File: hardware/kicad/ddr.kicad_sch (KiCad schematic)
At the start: 2 parts, among them U202 xc7z007sclg225, U301 MT41K256M16TW-107_P

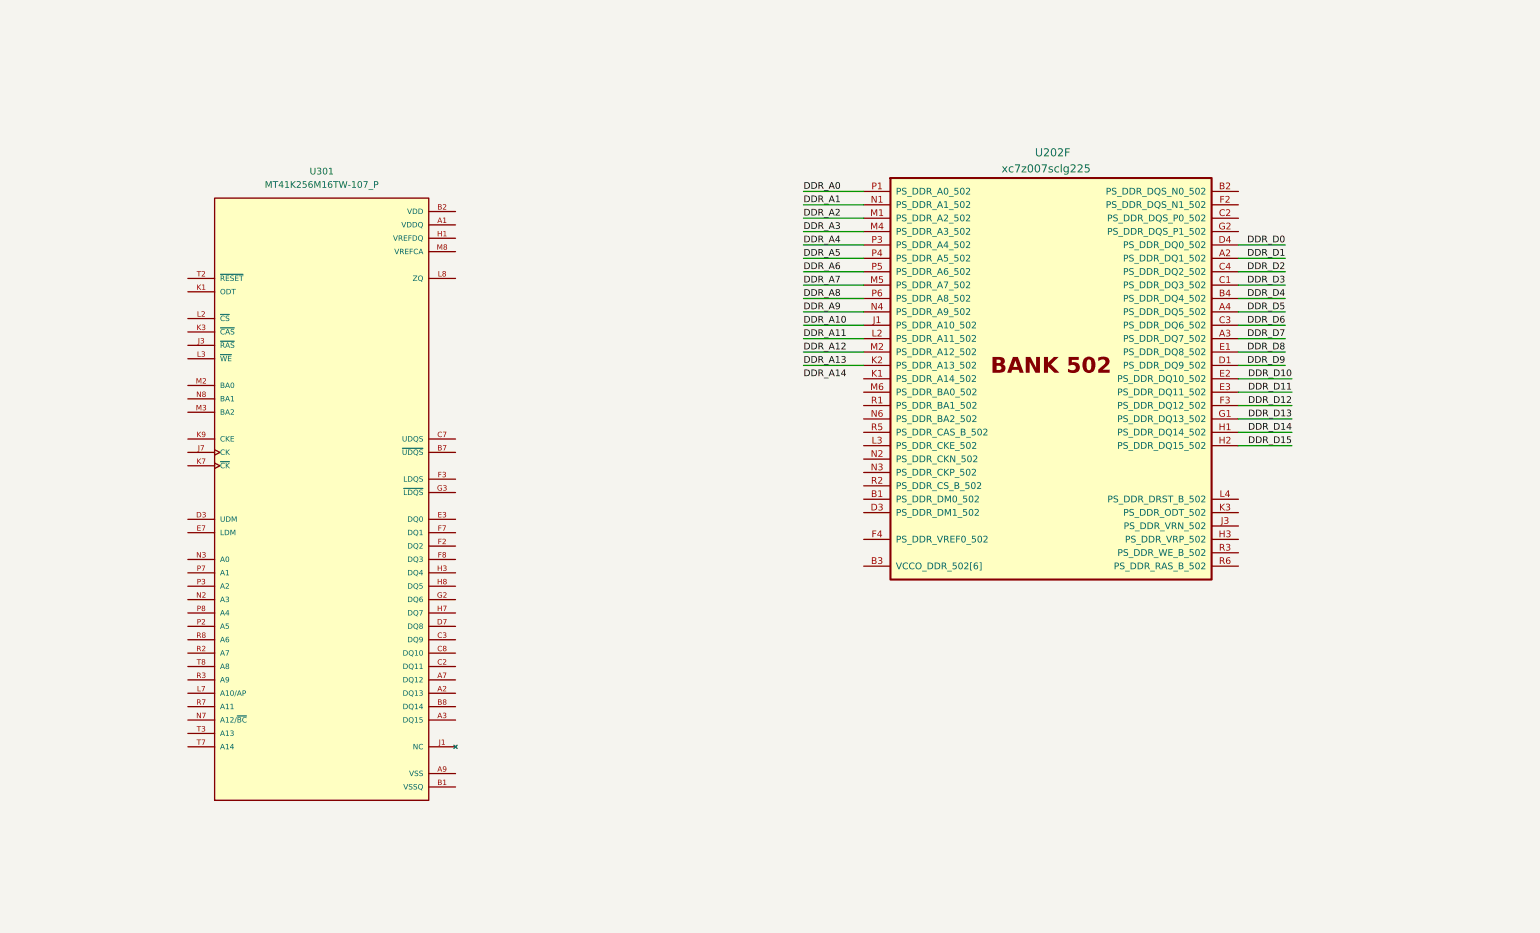
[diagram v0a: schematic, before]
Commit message: layout: finish dq0 & dq1 routing
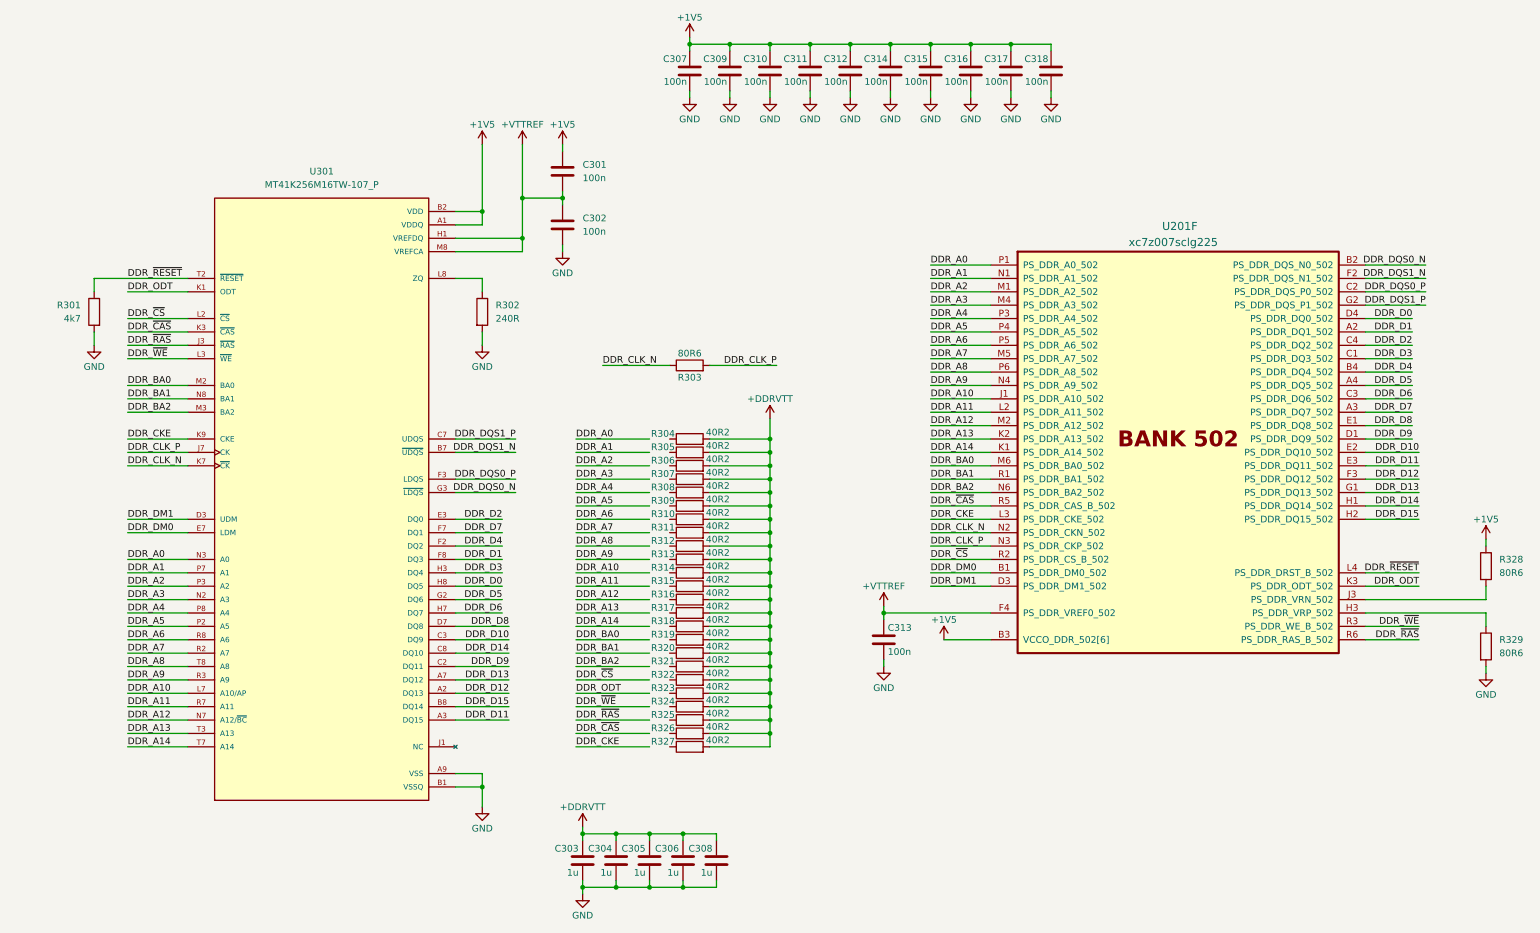
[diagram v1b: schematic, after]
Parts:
- added C301, C302, C307, C309, C310, C311, C312, C313, C314, C315, C316, C317, C318: 100n, Capacitor_SMD:C_0402_1005Metric, symbol Device:C
- added C303, C304, C305, C306, C308: 1u, Capacitor_SMD:C_0603_1608Metric, symbol Device:C
- added R301: 4k7, Resistor_SMD:R_0402_1005Metric, symbol Device:R
- added R302: 240R, Resistor_SMD:R_0402_1005Metric, symbol Device:R
- added R303, R328, R329: 80R6, Resistor_SMD:R_0402_1005Metric, symbol Device:R
- added R304, R305, R306, R307, R308, R309, R310, R311, R312, R313, R314, R315, R316, R317, R318, R319, R320, R321, R322, R323, R324, R325, R326, R327: 40R2, Resistor_SMD:R_0402_1005Metric, symbol Device:R
- U201: renamed from U202; footprint (none) -> Package_BGA:Xilinx_CLG225
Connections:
- net VDD is gone; now on net +1V5: U301.B2 (VDD), U301.D9 (VDD), U301.G7 (VDD), U301.K2 (VDD), U301.K8 (VDD), U301.N1 (VDD), U301.N9 (VDD), U301.R1 (VDD), U301.R9 (VDD)
- net VDDQ is gone; now on net +1V5: U301.A1 (VDDQ), U301.A8 (VDDQ), U301.C1 (VDDQ), U301.C9 (VDDQ), U301.D2 (VDDQ), U301.E9 (VDDQ), U301.F1 (VDDQ), U301.H2 (VDDQ), U301.H9 (VDDQ)
- net VSSQ is gone; now on net GND: U301.B1 (VSSQ), U301.B9 (VSSQ), U301.D1 (VSSQ), U301.D8 (VSSQ), U301.E2 (VSSQ), U301.E8 (VSSQ), U301.F9 (VSSQ), U301.G1 (VSSQ), U301.G9 (VSSQ)
- net DDR_A0: now also U301.N3 (A0)
- net DDR_A1: now also U301.P7 (A1)
- net DDR_A10: now also U301.L7 (A10/AP)
- net DDR_A11: now also U301.R7 (A11)
- net DDR_A12: now also U301.N7 (A12/~{BC})
- net DDR_A13: now also U301.T3 (A13)
- net DDR_A14: now also U201.K1 (PS_DDR_A14_502), U301.T7 (A14)
- net DDR_A2: now also U301.P3 (A2)
- net DDR_A3: now also U301.N2 (A3)
- net DDR_A4: now also U301.P8 (A4)
- net DDR_A5: now also U301.P2 (A5)
- net DDR_A6: now also U301.R8 (A6)
- net DDR_A7: now also U301.R2 (A7)
- net DDR_A8: now also U301.T8 (A8)
- net DDR_A9: now also U301.R3 (A9)
- net DDR_D0: now also U301.H8 (DQ5)
- net DDR_D1: now also U301.F8 (DQ3)
- net DDR_D10: now also U301.C3 (DQ9)
- net DDR_D11: now also U301.A3 (DQ15)
- net DDR_D12: now also U301.A2 (DQ13)
- net DDR_D13: now also U301.A7 (DQ12)
- net DDR_D14: now also U301.C8 (DQ10)
- net DDR_D15: now also U301.B8 (DQ14)
- net DDR_D2: now also U301.E3 (DQ0)
- net DDR_D3: now also U301.H3 (DQ4)
- net DDR_D4: now also U301.F2 (DQ2)
- net DDR_D5: now also U301.G2 (DQ6)
- net DDR_D6: now also U301.H7 (DQ7)
- net DDR_D7: now also U301.F7 (DQ1)
- net DDR_D8: now also U301.D7 (DQ8)
- net DDR_D9: now also U301.C2 (DQ11)
- net DDR_DQS1_N: now reaches U301.B7 (~{UDQS})
- net DDR_DQS1_N: now also U201.F2 (PS_DDR_DQS_N1_502)
- net DDR_DQS1_P: now reaches U301.C7 (UDQS)
- net DDR_DQS1_P: now also U201.G2 (PS_DDR_DQS_P1_502)
- net DDR_DM1: now reaches U301.D3 (UDM)
- net DDR_DM1: now also U201.D3 (PS_DDR_DM1_502)
- net DDR_DM0: now reaches U301.E7 (LDM)
- net DDR_DM0: now also U201.B1 (PS_DDR_DM0_502)
- net DDR_DQS0_P: now reaches U301.F3 (LDQS)
- net DDR_DQS0_P: now also U201.C2 (PS_DDR_DQS_P0_502)
- net DDR_DQS0_N: now reaches U301.G3 (~{LDQS})
- net DDR_DQS0_N: now also U201.B2 (PS_DDR_DQS_N0_502)
- net +VTTREF: now reaches U301.H1 (VREFDQ)
- net +VTTREF: now also U201.F4 (PS_DDR_VREF0_502), U301.M8 (VREFCA), C301.2, C302.1, C313.1
- net DDR_~{RAS}: now reaches U301.J3 (~{RAS})
- net DDR_~{RAS}: now also U201.R6 (PS_DDR_RAS_B_502)
- net DDR_CLK_P: now reaches U301.J7 (CK)
- net DDR_CLK_P: now also U201.N3 (PS_DDR_CKP_502), R303.2
- net DDR_ODT: now reaches U301.K1 (ODT)
- net DDR_ODT: now also U201.K3 (PS_DDR_ODT_502)
- net DDR_~{CAS}: now reaches U301.K3 (~{CAS})
- net DDR_~{CAS}: now also U201.R5 (PS_DDR_CAS_B_502)
- net DDR_CLK_N: now reaches U301.K7 (~{CK})
- net DDR_CLK_N: now also U201.N2 (PS_DDR_CKN_502), R303.1
- net DDR_CKE: now reaches U301.K9 (CKE)
- net DDR_CKE: now also U201.L3 (PS_DDR_CKE_502)
- net DDR_~{CS}: now reaches U301.L2 (~{CS})
- net DDR_~{CS}: now also U201.R2 (PS_DDR_CS_B_502)
- net DDR_~{WE}: now reaches U301.L3 (~{WE})
- net DDR_~{WE}: now also U201.R3 (PS_DDR_WE_B_502)
- net at U301.L8 (ZQ): now also R302.1
- net DDR_BA0: now reaches U301.M2 (BA0)
- net DDR_BA0: now also U201.M6 (PS_DDR_BA0_502)
- net DDR_BA2: now reaches U301.M3 (BA2)
- net DDR_BA2: now also U201.N6 (PS_DDR_BA2_502)
- net DDR_BA1: now reaches U301.N8 (BA1)
- net DDR_BA1: now also U201.R1 (PS_DDR_BA1_502)
- net DDR_~{RESET}: now reaches U301.T2 (~{RESET})
- net DDR_~{RESET}: now also U201.L4 (PS_DDR_DRST_B_502), R301.1
- net +1V5: now reaches U201.B3 (VCCO_DDR_502[6]), U201.E4 (VCCO_DDR_502[6]), U201.F1 (VCCO_DDR_502[6]), U201.J2 (VCCO_DDR_502[6]), U201.M3 (VCCO_DDR_502[6]), U201.R4 (VCCO_DDR_502[6])
- net +1V5: now also C301.1, C307.1, C309.1, C310.1, C311.1, C312.1, C314.1, C315.1, C316.1, C317.1, C318.1, R328.1
- net at U201.H3 (PS_DDR_VRP_502): now also R329.1
- net at U201.J3 (PS_DDR_VRN_502): now also R328.2
- net VSS renamed GND
- net GND: now also C302.2, C303.2, C304.2, C305.2, C306.2, C307.2, C308.2, C309.2, C310.2, C311.2, C312.2, C313.2, C314.2, C315.2, C316.2, C317.2, C318.2, R301.2, R302.2, R329.2
- new net +DDRVTT: C303.1, C304.1, C305.1, C306.1, C308.1, R304.2, R305.2, R306.2, R307.2, R308.2, R309.2, R310.2, R311.2, R312.2, R313.2, R314.2, R315.2, R316.2, R317.2, R318.2, R319.2, R320.2, R321.2, R322.2, R323.2, R324.2, R325.2, R326.2, R327.2
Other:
- moved on the sheet: U201F

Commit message: layout: finish ddr ctrl routing
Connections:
- net DDR_~{RESET}: no longer R301.1
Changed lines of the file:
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@@
-	(wire
-		(pts
-			(xy 30.48 67.31) (xy 30.48 64.77)
-		)
-		(stroke
-			(width 0)
-			(type default)
-		)
-	)
 	(wire
 		(pts

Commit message: pcb: complete FPGA and DDR BGA breakout
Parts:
- removed C303, C304, C305, C306, C308: 1u, Capacitor_SMD:C_0603_1608Metric, symbol Device:C
- removed R306, R307, R308, R309, R310, R311, R312, R313, R314, R315, R316, R317, R318, R319, R320, R321, R322, R323, R324, R325, R326, R327: 40R2, Resistor_SMD:R_0402_1005Metric, symbol Device:R
- R304, R305: value 40R2 -> 80R6
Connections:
- net +1V5: now also R304.1
- net +VTTREF: now also R304.2, R305.1
- net GND: now also R305.2
- removed net +DDRVTT: R304.2, R305.2

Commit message: feat: need switch two singals of SD inferface
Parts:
- added R306, R307: 80R6, Resistor_SMD:R_0402_1005Metric, symbol Device:R
- U201: footprint Package_BGA:Xilinx_CLG225 -> (none)
- U301: footprint Projects:BGA96C80P9X16_1400X800X120 -> Project:BGA96C80P9X16_1400X800X120
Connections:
- net +1V5: now also R306.1
- net DDR_~{RESET}: now also R301.1
- net GND: now also R307.2
- net +VTTREF renamed DDR3_VREF
- net DDR3_VREF: no longer C313.1, U201.F4 (PS_DDR_VREF0_502)
- new net ZYNQ_DDR_VREF: C313.1, R306.2, R307.1, U201.F4 (PS_DDR_VREF0_502)
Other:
- moved on the sheet: C301, C302, C307, C309, C310, C311, C312, C313, C314, C315, C316, C317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
